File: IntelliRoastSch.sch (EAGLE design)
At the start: 69 parts, among them IC11 MAX31855, IC7 MAX31855, IC9 MAX31855, J1 1X2-3.5MM, J2 1X2-3.5MM, J3 1X2-3.5MM, J4 1X2-3.5MM, J5 1X2-3.5MM, J6 1X2-3.5MM, J7 1X2-3.5MM, U1 LM2576HVS-3.3/NOPB, U2 MOUDLE-BLUETOOTH-HC-05(34P-27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

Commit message: Should click save before commiting changes
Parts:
- removed -TSSOP1: MAX3221-TSSOP16, MAX3221:MAX3221-TSSOP16
- removed C10, C11, C12, C13, C14: 0.1uF, eagle-ltspice:CC0603
- removed J1, J2: 1X2-3.5MM, adafruit:1X2-3.5MM
- removed Q1: (no value), transistor-power:PMOSFET_NTO220BH
- removed R1: 1000, rcl:R-US_R0603
- removed R7, R8: 0, adafruit:R-US_R0805
- removed U2: MOUDLE-BLUETOOTH-HC-05(34P-27X13MM), MOUDLE-BLUETOOTH-HC-05_34P-27X13MM_:MOUDLE-BLUETOOTH-HC-05(34P-27X13MM)
- added BT_HEADER: (no value), pinhead:PINHD-1X6
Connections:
- removed net BT_UART_RX: -TSSOP1.DOUT, R8.1
- removed net BT_UART_TX: -TSSOP1.RIN, R7.1
- removed net C1+: -TSSOP1.C1+, C12.1
- removed net C1-: -TSSOP1.C1-, C12.2
- removed net C2+: -TSSOP1.C2+, C13.1
- removed net C2-: -TSSOP1.C2-, C13.2
- removed net DRAIN: J1.1, Q1.D
- removed net GATE: Q1.G, R1.2
- removed net KEY: U2.PIO[11]
- removed net N$21: -TSSOP1.V+, C10.1
- removed net N$22: -TSSOP1.V-, C11.1
- removed net N$23: R7.2, U2.UART-TX
- removed net N$24: R8.2, U2.UART-RX
- removed net N$3: Q2.G, R2.2
- removed net PWR: J1.2, J2.2
- removed net SOURCE: J2.1, Q1.S, R1.1
- removed net STM_RX: -TSSOP1.ROUT
- removed net STM_TX: -TSSOP1.DIN
- new net BT_ENABLE: BT_HEADER.1
- new net BT_STATE: BT_HEADER.6
- net +3V3: now also BT_HEADER.2; no longer -TSSOP1.FORCEON, -TSSOP1.VCC, -TSSOP1.\!FORCEOFF, C14.2, U2.3.3V
- net BT_RX: now also BT_HEADER.4
- net BT_TX: now also BT_HEADER.5
- net GND: now also BT_HEADER.3; no longer -TSSOP1.GND, -TSSOP1.\!EN, C10.2, C11.2, C14.1, U2.GND0, U2.GND1, U2.GND2, U2.GND3
- net TIM3_CH1: now also Q2.G, R2.2
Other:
- note removed: "TODO: - Change out caps to "Adafruit" equivalent for consistancy - Double check wiring - Add a way to get into programming mode so we can change the BT Name to "IntelliRoast" -Add parts to BOM"

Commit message: added headers for thermocouples.
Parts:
- removed C15, C16, C18, C19, C21, C22: 10uF, adafruit:C-USC0805K
- removed C17, C20, C23: 0.01µF, microbuilder:CAP_CERAMIC_0805
- removed D10, D12, D8: 1N4148, adafruit:DIODESOD-323F
- removed D11, D7, D9: 1n4148, adafruit:DIODESOD-323F
- removed FB10, FB11, FB12, FB7, FB8, FB9: Ferrite, microbuilder:FERRITE_0805
- removed IC11, IC7, IC9: MAX31855, adafruit:MAX6675
- removed J4, J5, J6: 1X2-3.5MM, adafruit:1X2-3.5MM
- removed JP10, JP9: Breakout, microbuilder:HEADER-1X676MIL
- removed R10, R11, R12, R13, R14, R9: 10K, adafruit:R-US_R0805
- added JP1, JP2, JP3: (no value), pinhead:PINHD-1X6
- JP8: value Breakout -> (none); device microbuilder:HEADER-1X676MIL -> pinhead:PINHD-1X6
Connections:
- removed net +5V: JP10.1, JP8.1, JP9.1
- removed net CS3: D8.A, IC7./CS, R10.2
- removed net CS4: D10.A, IC9./CS, R12.2
- removed net CS5: D12.A, IC11./CS, R14.2
- removed net DO3: IC7.DO, JP8.4
- removed net DO4: IC9.DO, JP9.4
- removed net DO5: IC11.DO, JP10.4
- removed net N$103: D9.C, JP9.6
- removed net N$119: FB9.P$1, J5.2
- removed net N$120: C20.P$1, FB9.P$2, IC9.T-
- removed net N$121: FB10.P$1, J5.1
- removed net N$122: C20.P$2, FB10.P$2, IC9.T+
- removed net N$123: D12.C, JP10.5
- removed net N$124: D11.C, JP10.6
- removed net N$125: FB11.P$1, J6.2
- removed net N$126: C23.P$1, FB11.P$2, IC11.T-
- removed net N$127: FB12.P$1, J6.1
- removed net N$128: C23.P$2, FB12.P$2, IC11.T+
- removed net N$39: D8.C, JP8.5
- removed net N$66: D7.C, JP8.6
- removed net N$69: FB7.P$1, J4.2
- removed net N$75: C17.P$1, FB7.P$2, IC7.T-
- removed net N$83: FB8.P$1, J4.1
- removed net N$84: C17.P$2, FB8.P$2, IC7.T+
- removed net N$99: D10.C, JP9.5
- removed net SCK3: D7.A, IC7.SCK, R9.2
- removed net SCK4: D9.A, IC9.SCK, R11.2
- removed net SCK5: D11.A, IC11.SCK, R13.2
- net +3V3: now also JP1.6, JP2.6, JP3.6, JP8.6; no longer C15.1, C16.1, C18.1, C19.1, C21.1, C22.1, IC11.VCC, IC7.VCC, IC9.VCC, JP10.2, JP8.2, JP9.2, R10.1, R11.1, R12.1, R13.1, R14.1, R9.1
- net GND: now also JP1.4, JP2.4, JP3.4, JP8.4; no longer C15.2, C16.2, C18.2, C19.2, C21.2, C22.2, IC11.GND, IC7.GND, IC9.GND, JP10.3, JP8.3, JP9.3
- net SPI1_CS2: now also JP1.2
- net SPI1_CS3: now also JP8.2
- net SPI1_MISO: now also JP1.3, JP2.3, JP3.3, JP8.3
- net SPI1_SCK: now also JP1.1, JP2.1, JP3.1, JP8.1
- net SPI2_CS0: now also JP2.2
- net SPI2_CS1: now also JP3.2
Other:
- note added: "TODO: -Add Parts to BOM"
- note removed: "TODO: -Remove Header pins and tie directly into STM32F207 Spi bus -Double check all the parts have the correct footprints -Remove any 5V rails -Add Parts to BOM"

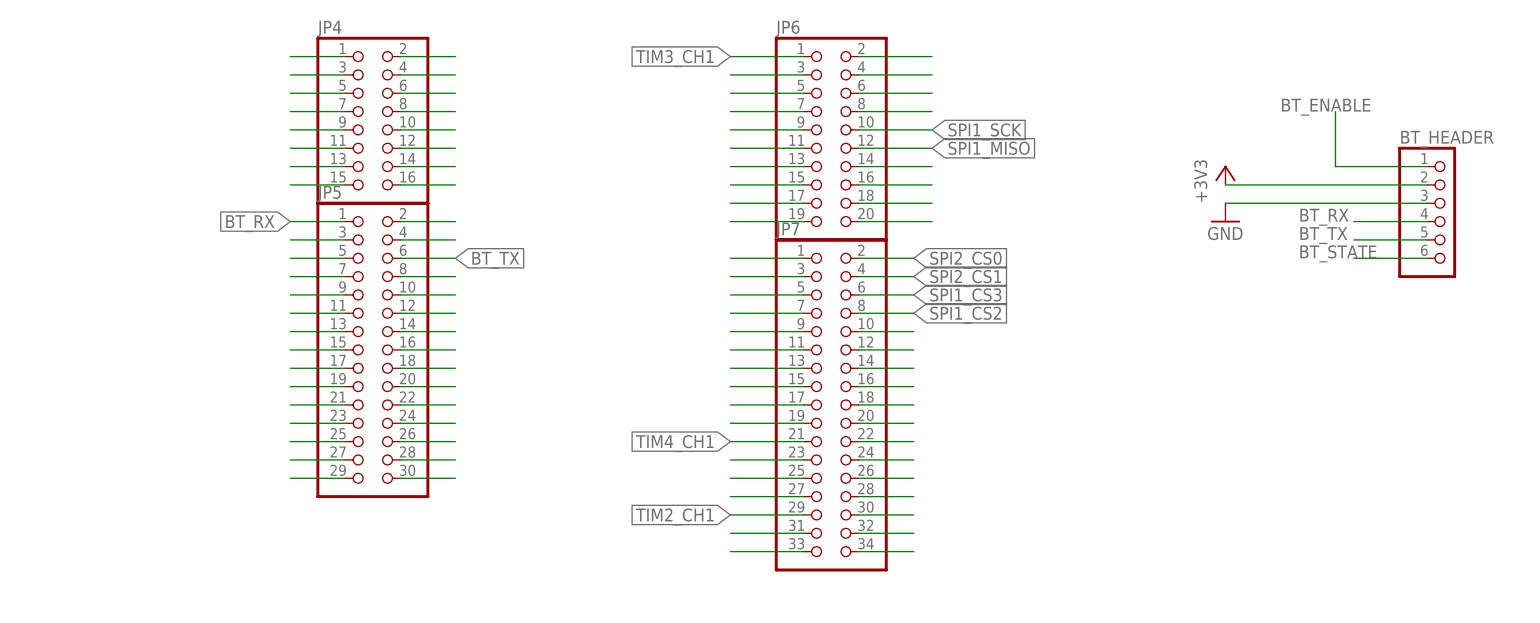
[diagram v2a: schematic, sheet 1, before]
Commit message: Added header for Microphone
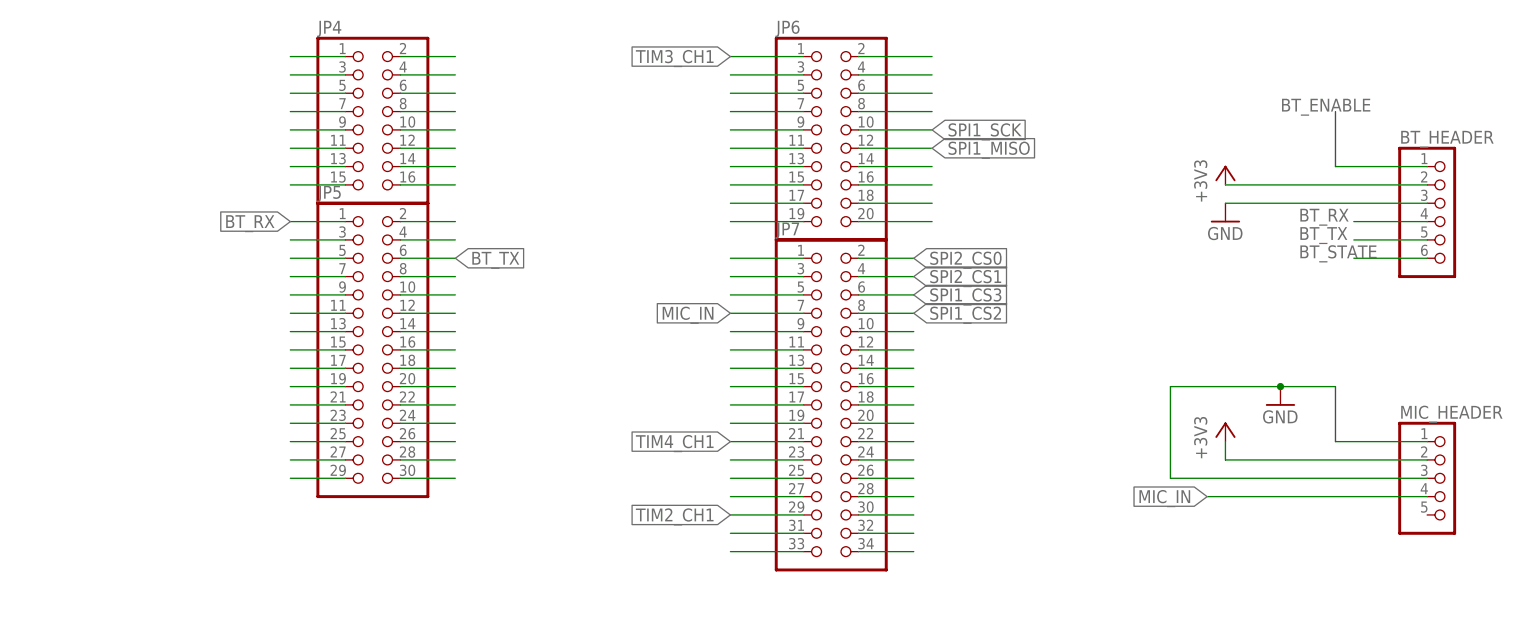
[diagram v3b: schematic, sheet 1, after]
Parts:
- added MIC_HEADER: (no value), pinhead:PINHD-1X5
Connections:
- removed net N$92: JP7.7
- new net MIC_IN: JP7.7, MIC_HEADER.4
- net +3V3: now also MIC_HEADER.2
- net GND: now also MIC_HEADER.1, MIC_HEADER.3
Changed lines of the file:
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@@
 <?xml version="1.0" encoding="utf-8"?>
 <!DOCTYPE eagle SYSTEM "eagle.dtd">
-<eagle version="9.3.0">
+<eagle version="9.3.1">
 <drawing>
 <settings>
-<setting alwaysvectorfont="no"/>
+<setting alwaysvectorfont="yes"/>
 <setting verticaltext="up"/>
 </settings>
@@
 <part name="+3V6" library="supply1" library_urn="urn:adsk.eagle:library:371" deviceset="+3V3" device=""/>
 <part name="+3V7" library="supply1" library_urn="urn:adsk.eagle:library:371" deviceset="+3V3" device=""/>
+<part name="MIC_HEADER" library="pinhead" library_urn="urn:adsk.eagle:library:325" deviceset="PINHD-1X5" device="" package3d_urn="urn:adsk.eagle:package:22469/2"/>
+<part name="GND12" library="supply1" library_urn="urn:adsk.eagle:library:371" deviceset="GND" device=""/>
+<part name="+3V8" library="supply1" library_urn="urn:adsk.eagle:library:371" deviceset="+3V3" device=""/>
 </parts>
 <sheets>
@@
 <attribute name="VALUE" x="22.86" y="119.38" size="1.778" layer="96"/>
 </instance>
+<instance part="MIC_HEADER" gate="A" x="55.88" y="86.36" smashed="yes">
+<attribute name="NAME" x="49.53" y="94.615" size="1.778" layer="95"/>
+<attribute name="VALUE" x="49.53" y="76.2" size="1.778" layer="96"/>
+</instance>
+<instance part="GND12" gate="1" x="33.02" y="96.52" smashed="yes">
+<attribute name="VALUE" x="30.48" y="93.98" size="1.778" layer="96"/>
+</instance>
+<instance part="+3V8" gate="G$1" x="25.4" y="93.98" smashed="yes">
+<attribute name="VALUE" x="22.86" y="88.9" size="1.778" layer="96" rot="R90"/>
+</instance>
 </instances>
 <busses>
@@
 </segment>
 </net>
-<net name="N$92" class="0">
+<net name="MIC_IN" class="0">
 <segment>
 <pinref part="JP7" gate="G$1" pin="7"/>
 <wire x1="-33.02" y1="109.22" x2="-43.18" y2="109.22" width="0.1524" layer="91"/>
+<label x="-43.18" y="109.22" size="1.778" layer="95" rot="R180" xref="yes"/>
+</segment>
+<segment>
+<pinref part="MIC_HEADER" gate="A" pin="4"/>
+<wire x1="53.34" y1="83.82" x2="22.86" y2="83.82" width="0.1524" layer="91"/>
+<label x="22.86" y="83.82" size="1.778" layer="95" rot="R180" xref="yes"/>
 </segment>
 </net>
@@
 <wire x1="25.4" y1="127" x2="53.34" y2="127" width="0.1524" layer="91"/>
 </segment>
+<segment>
+<pinref part="MIC_HEADER" gate="A" pin="2"/>
+<pinref part="+3V8" gate="G$1" pin="+3V3"/>
+<wire x1="53.34" y1="88.9" x2="25.4" y2="88.9" width="0.1524" layer="91"/>
+<wire x1="25.4" y1="88.9" x2="25.4" y2="91.44" width="0.1524" layer="91"/>
+</segment>
 </net>
 <net name="GND" class="0">
@@
 <wire x1="25.4" y1="124.46" x2="53.34" y2="124.46" width="0.1524" layer="91"/>
 </segment>
-</net>
+<segment>
+<pinref part="MIC_HEADER" gate="A" pin="1"/>
+<wire x1="53.34" y1="91.44" x2="40.64" y2="91.44" width="0.1524" layer="91"/>
+<wire x1="40.64" y1="91.44" x2="40.64" y2="99.06" width="0.1524" layer="91"/>
+<pinref part="GND12" gate="1" pin="GND"/>
+<wire x1="40.64" y1="99.06" x2="33.02" y2="99.06" width="0.1524" layer="91"/>
+<pinref part="MIC_HEADER" gate="A" pin="3"/>
+<wire x1="53.34" y1="86.36" x2="17.78" y2="86.36" width="0.1524" layer="91"/>
+<wire x1="17.78" y1="86.36" x2="17.78" y2="99.06" width="0.1524" layer="91"/>
+<wire x1="17.78" y1="99.06" x2="33.02" y2="99.06" width="0.1524" layer="91"/>
+<junction x="33.02" y="99.06"/>
+</segment>
+</net>

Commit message: Started working on Board
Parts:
- removed JP5: (no value), pinhead:PINHD-2X15
- removed JP7: (no value), pinhead:PINHD-2X17
- added CN10: (no value), pinhead:PINHD-2X17
- added CN9: (no value), pinhead:PINHD-2X15
- renumbered J3 to 12V_TERM, J7 to FAN_TERM, JP4 to CN8, JP6 to CN7
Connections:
- net N$2 renamed FAN_TO_MOS
- removed net N$19: CN8.1
- net BT_RX: now also CN9.1; no longer JP5.1
- net BT_TX: now also CN9.6; no longer JP5.6
- net MIC_IN: now also CN10.7; no longer JP7.7
- net N$100: now also CN10.23; no longer JP7.23
- net N$101: now also CN10.25; no longer JP7.25
- net N$102: now also CN10.27; no longer JP7.27
- net N$104: now also CN10.31; no longer JP7.31
- net N$105: now also CN10.33; no longer JP7.33
- net N$106: now also CN10.34; no longer JP7.34
- net N$107: now also CN10.32; no longer JP7.32
- net N$108: now also CN10.30; no longer JP7.30
- net N$109: now also CN10.28; no longer JP7.28
- net N$110: now also CN10.26; no longer JP7.26
- net N$111: now also CN10.24; no longer JP7.24
- net N$112: now also CN10.22; no longer JP7.22
- net N$113: now also CN10.20; no longer JP7.20
- net N$114: now also CN10.18; no longer JP7.18
- net N$115: now also CN10.16; no longer JP7.16
- net N$116: now also CN10.14; no longer JP7.14
- net N$117: now also CN10.12; no longer JP7.12
- net N$118: now also CN10.10; no longer JP7.10
- net N$40: now also CN9.3; no longer JP5.3
- net N$41: now also CN9.5; no longer JP5.5
- net N$42: now also CN9.7; no longer JP5.7
- net N$43: now also CN9.9; no longer JP5.9
- net N$44: now also CN9.11; no longer JP5.11
- net N$45: now also CN8.1, CN9.13; no longer JP5.13
- net N$46: now also CN9.15; no longer JP5.15
- net N$47: now also CN9.17; no longer JP5.17
- net N$48: now also CN9.19; no longer JP5.19
- net N$49: now also CN9.21; no longer JP5.21
- net N$50: now also CN9.23; no longer JP5.23
- net N$51: now also CN9.25; no longer JP5.25
- net N$52: now also CN9.27; no longer JP5.27
- net N$53: now also CN9.29; no longer JP5.29
- net N$54: now also CN9.30; no longer JP5.30
- net N$55: now also CN9.28; no longer JP5.28
- net N$56: now also CN9.26; no longer JP5.26
- net N$57: now also CN9.24; no longer JP5.24
- net N$58: now also CN9.22; no longer JP5.22
- net N$59: now also CN9.20; no longer JP5.20
- net N$60: now also CN9.18; no longer JP5.18
- net N$61: now also CN9.16; no longer JP5.16
- net N$62: now also CN9.14; no longer JP5.14
- net N$63: now also CN9.12; no longer JP5.12
- net N$64: now also CN9.10; no longer JP5.10
- net N$65: now also CN9.8; no longer JP5.8
- net N$67: now also CN9.4; no longer JP5.4
- net N$68: now also CN9.2; no longer JP5.2
- net N$89: now also CN10.1; no longer JP7.1
- net N$90: now also CN10.3; no longer JP7.3
- net N$91: now also CN10.5; no longer JP7.5
- net N$93: now also CN10.9; no longer JP7.9
- net N$94: now also CN10.11; no longer JP7.11
- net N$95: now also CN10.13; no longer JP7.13
- net N$96: now also CN10.15; no longer JP7.15
- net N$97: now also CN10.17; no longer JP7.17
- net N$98: now also CN10.19; no longer JP7.19
- net SPI1_CS2: now also CN10.8; no longer JP7.8
- net SPI1_CS3: now also CN10.6; no longer JP7.6
- net SPI2_CS0: now also CN10.2; no longer JP7.2
- net SPI2_CS1: now also CN10.4; no longer JP7.4
- net TIM2_CH1: now also CN10.29; no longer JP7.29
- net TIM4_CH1: now also CN10.21; no longer JP7.21

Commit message: added power and ground connections to F207 Headers, connected BT pins to F207 Headers, Added jumpers to configure power delivery to F207
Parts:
- added EXT_12V, EXT_3V3: (no value), pinhead:PINHD-1X2
- renumbered JP1 to TEMP2, JP2 to TEMP0, JP3 to TEMP1, JP8 to TEMP3
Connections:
- removed net N$100: CN10.23
- removed net N$101: CN10.25
- removed net N$102: CN10.27
- removed net N$104: CN10.31
- removed net N$105: CN10.33
- removed net N$106: CN10.34
- removed net N$107: CN10.32
- removed net N$108: CN10.30
- removed net N$109: CN10.28
- removed net N$110: CN10.26
- removed net N$111: CN10.24
- removed net N$112: CN10.22
- removed net N$113: CN10.20
- removed net N$114: CN10.18
- removed net N$115: CN10.16
- removed net N$116: CN10.14
- removed net N$117: CN10.12
- removed net N$118: CN10.10
- removed net N$20: CN8.3
- removed net N$25: CN8.5
- removed net N$26: CN8.7
- removed net N$27: CN8.9
- removed net N$28: CN8.11
- removed net N$29: CN8.13
- removed net N$30: CN8.15
- removed net N$31: CN8.16
- removed net N$32: CN8.14
- removed net N$33: CN8.12
- removed net N$34: CN8.10
- removed net N$35: CN8.8
- removed net N$36: CN8.6
- removed net N$37: CN8.4
- removed net N$38: CN8.2
- removed net N$40: CN9.3
- removed net N$41: CN9.5
- removed net N$42: CN9.7
- removed net N$43: CN9.9
- removed net N$44: CN9.11
- removed net N$45: CN8.1, CN9.13
- removed net N$46: CN9.15
- removed net N$47: CN9.17
- removed net N$48: CN9.19
- removed net N$49: CN9.21
- removed net N$50: CN9.23
- removed net N$51: CN9.25
- removed net N$52: CN9.27
- removed net N$53: CN9.29
- removed net N$54: CN9.30
- removed net N$55: CN9.28
- removed net N$56: CN9.26
- removed net N$57: CN9.24
- removed net N$58: CN9.22
- removed net N$59: CN9.20
- removed net N$60: CN9.18
- removed net N$61: CN9.16
- removed net N$62: CN9.14
- removed net N$63: CN9.12
- removed net N$64: CN9.10
- removed net N$65: CN9.8
- removed net N$67: CN9.4
- removed net N$68: CN9.2
- removed net N$70: CN7.3
- removed net N$71: CN7.5
- removed net N$72: CN7.7
- removed net N$73: CN7.9
- removed net N$74: CN7.11
- removed net N$76: CN7.15
- removed net N$77: CN7.17
- removed net N$78: CN7.19
- removed net N$79: CN7.2
- removed net N$80: CN7.4
- removed net N$81: CN7.6
- removed net N$82: CN7.8
- removed net N$85: CN7.14
- removed net N$86: CN7.16
- removed net N$87: CN7.18
- removed net N$88: CN7.20
- removed net N$89: CN10.1
- removed net N$90: CN10.3
- removed net N$91: CN10.5
- removed net N$93: CN10.9
- removed net N$94: CN10.11
- removed net N$95: CN10.13
- removed net N$96: CN10.15
- removed net N$97: CN10.17
- removed net N$98: CN10.19
- removed net SPI1_MOSI: CN7.13
- new net N$2: CN8.7, EXT_3V3.2
- new net N$3: CN8.15, EXT_12V.2
- net +12V: now also EXT_12V.1
- net +3V3: now also EXT_3V3.1
- net BT_ENABLE: now also CN10.10
- net BT_STATE: now also CN10.12
- net GND: now also CN10.15, CN10.17, CN10.22, CN10.27, CN10.5, CN7.8, CN8.11, CN8.13, CN9.12, CN9.23

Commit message: Arranged the components on board, need to add gnd, 3v3, 12v, and gnd planes and then start to route board
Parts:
- C1, C5: value (none) -> 100uF
- C2, C6: value (none) -> 10uF
- C3, C4, C7, C8: value (none) -> 0.1uF
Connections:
- net N$1 renamed OUT
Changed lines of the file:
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@@
 <part name="U1" library="LM2576HVS-3.3_NOPB" deviceset="LM2576HVS-3.3/NOPB" device=""/>
 <part name="D1" library="eagle-ltspice" library_urn="urn:adsk.eagle:library:217" deviceset="SCHOTTKY-DIODE" device="SMC" package3d_urn="urn:adsk.eagle:package:13317/1"/>
-<part name="C1" library="adafruit" library_urn="urn:adsk.eagle:library:420" deviceset="C-US" device="C1210" package3d_urn="urn:adsk.eagle:package:6240334/1"/>
-<part name="C2" library="adafruit" library_urn="urn:adsk.eagle:library:420" deviceset="C-US" device="C0805" package3d_urn="urn:adsk.eagle:package:6240337/1"/>
-<part name="C3" library="adafruit" library_urn="urn:adsk.eagle:library:420" deviceset="C-US" device="C0603" package3d_urn="urn:adsk.eagle:package:6240338/1"/>
-<part name="C4" library="adafruit" library_urn="urn:adsk.eagle:library:420" deviceset="C-US" device="C0603" package3d_urn="urn:adsk.eagle:package:6240338/1"/>
+<part name="C1" library="adafruit" library_urn="urn:adsk.eagle:library:420" deviceset="C-US" device="C1210" package3d_urn="urn:adsk.eagle:package:6240334/1" value="100uF"/>
+<part name="C2" library="adafruit" library_urn="urn:adsk.eagle:library:420" deviceset="C-US" device="C0805" package3d_urn="urn:adsk.eagle:package:6240337/1" value="10uF"/>
+<part name="C3" library="adafruit" library_urn="urn:adsk.eagle:library:420" deviceset="C-US" device="C0603" package3d_urn="urn:adsk.eagle:package:6240338/1" value="0.1uF"/>
+<part name="C4" library="adafruit" library_urn="urn:adsk.eagle:library:420" deviceset="C-US" device="C0603" package3d_urn="urn:adsk.eagle:package:6240338/1" value="0.1uF"/>
 <part name="L1" library="IntelliRoast" deviceset="L" device="POWER_REGULATOR"/>
 <part name="+3V1" library="supply1" library_urn="urn:adsk.eagle:library:371" deviceset="+3V3" device=""/>
-<part name="C5" library="adafruit" library_urn="urn:adsk.eagle:library:420" deviceset="C-US" device="C1210" package3d_urn="urn:adsk.eagle:package:6240334/1"/>
-<part name="C6" library="adafruit" library_urn="urn:adsk.eagle:library:420" deviceset="C-US" device="C0805" package3d_urn="urn:adsk.eagle:package:6240337/1"/>
-<part name="C7" library="adafruit" library_urn="urn:adsk.eagle:library:420" deviceset="C-US" device="C0603" package3d_urn="urn:adsk.eagle:package:6240338/1"/>
-<part name="C8" library="adafruit" library_urn="urn:adsk.eagle:library:420" deviceset="C-US" device="C0603" package3d_urn="urn:adsk.eagle:package:6240338/1"/>
+<part name="C5" library="adafruit" library_urn="urn:adsk.eagle:library:420" deviceset="C-US" device="C1210" package3d_urn="urn:adsk.eagle:package:6240334/1" value="100uF"/>
+<part name="C6" library="adafruit" library_urn="urn:adsk.eagle:library:420" deviceset="C-US" device="C0805" package3d_urn="urn:adsk.eagle:package:6240337/1" value="10uF"/>
+<part name="C7" library="adafruit" library_urn="urn:adsk.eagle:library:420" deviceset="C-US" device="C0603" package3d_urn="urn:adsk.eagle:package:6240338/1" value="0.1uF"/>
+<part name="C8" library="adafruit" library_urn="urn:adsk.eagle:library:420" deviceset="C-US" device="C0603" package3d_urn="urn:adsk.eagle:package:6240338/1" value="0.1uF"/>
 <part name="FRAME4" library="frames" library_urn="urn:adsk.eagle:library:229" deviceset="FRAME_A_L" device=""/>
 <part name="FRAME5" library="frames" library_urn="urn:adsk.eagle:library:229" deviceset="FRAME_A_L" device=""/>
@@
 <wire x1="-104.14" y1="134.62" x2="-104.14" y2="132.08" width="0.1524" layer="91"/>
 <pinref part="CN8" gate="A" pin="11"/>
+<wire x1="-104.14" y1="132.08" x2="-96.52" y2="132.08" width="0.1524" layer="91"/>
 <pinref part="CN8" gate="A" pin="13"/>
-<wire x1="-96.52" y1="129.54" x2="-96.52" y2="132.08" width="0.1524" layer="91"/>
-<wire x1="-104.14" y1="132.08" x2="-96.52" y2="132.08" width="0.1524" layer="91"/>
+<wire x1="-96.52" y1="129.54" x2="-104.14" y2="129.54" width="0.1524" layer="91"/>
+<wire x1="-104.14" y1="129.54" x2="-104.14" y2="132.08" width="0.1524" layer="91"/>
+<junction x="-104.14" y="132.08"/>
 </segment>
 </net>
@@
 </segment>
 </net>
-<net name="N$1" class="0">
+<net name="OUT" class="0">
 <segment>
 <pinref part="L1" gate="G$1" pin="1"/>
@@
 </sheet>
 </sheets>
+<errors>
+</errors>
 </schematic>
 </drawing>
